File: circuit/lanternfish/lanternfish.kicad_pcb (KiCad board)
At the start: 2 copper layers, 100 x 70 mm, 56 parts, among them J1 Input, J2 Prog, J3 Output, Q1 FQD17P06TM, Q2 PSMN5R6-60YLX, Q3 SI2302DDS-T1-GE3, SW1 SW_Push, SW2 SW_Push, SW3 PEC11R-4215F-S0024, SW6 SW_SPST, U1 MCP7940N-xMS, U2 L7805, U3 ATmega328PB-AU, Y1 ABS25-32.768KHZ-6-1-T

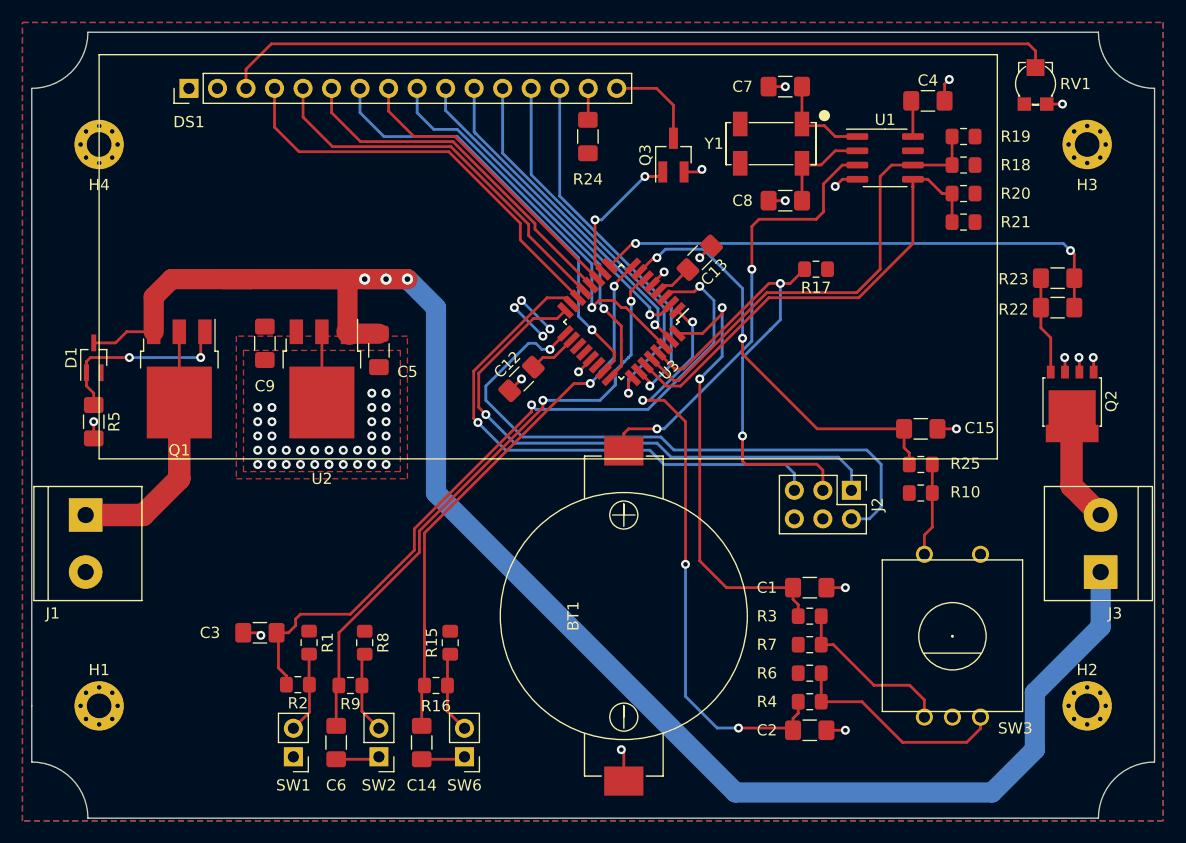
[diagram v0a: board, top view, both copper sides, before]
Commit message: Updated LCD Fixations
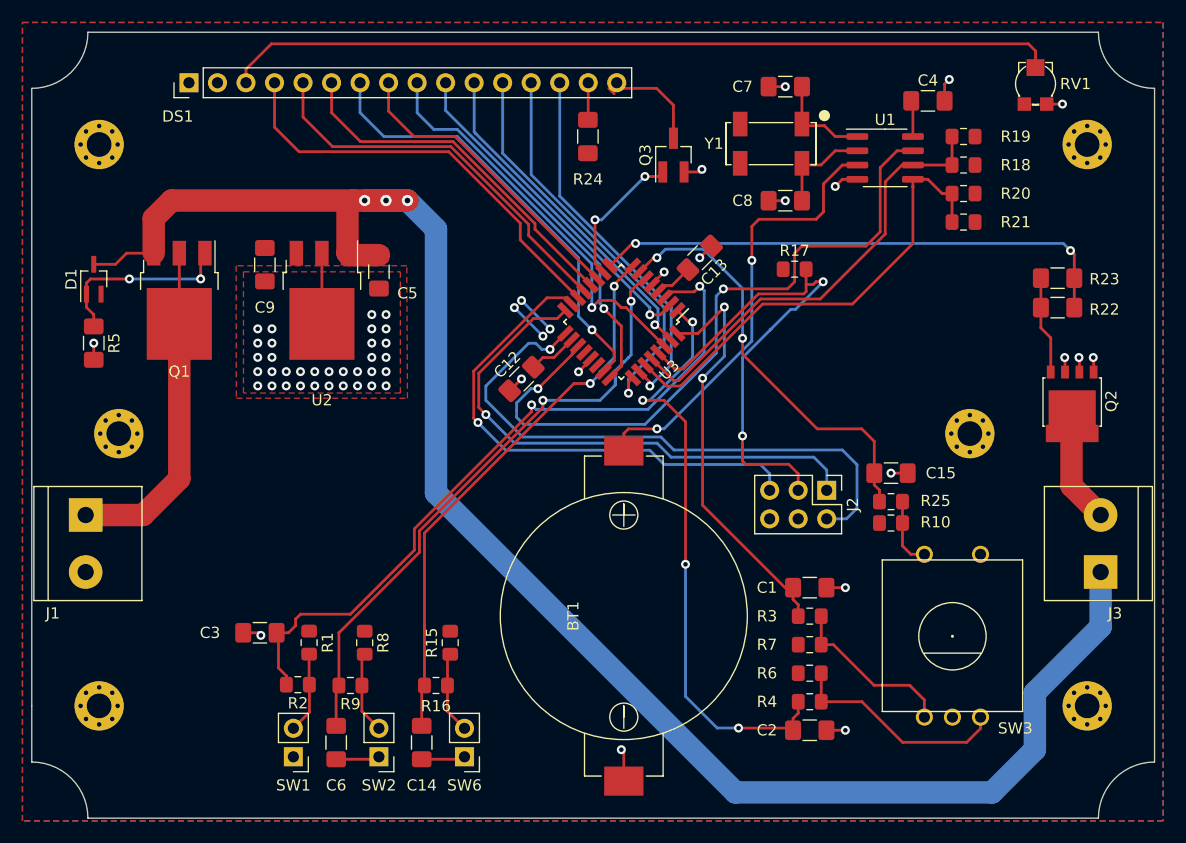
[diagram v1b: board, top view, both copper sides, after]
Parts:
- added REF**: MountingHole_2.2mm_M2_Pad_Via, MountingHole:MountingHole_2.2mm_M2_Pad_Via, F.Cu at (184.6, 95.8)
- added REF**: MountingHole_2.2mm_M2_Pad_Via, MountingHole:MountingHole_2.2mm_M2_Pad_Via, F.Cu at (108.8, 95.8)
- moved C5 7.00 mm to (131.9, 81.3)
- moved C9 7.00 mm to (121.8, 80.7)
- moved D1 7.00 mm to (106.5, 82.0)
- moved Q1 7.00 mm to (114.1, 83.9)
- moved R5 7.00 mm to (106.5, 87.7)
- moved U2 7.00 mm to (126.8, 83.9)
- moved C15 4.76 mm to (177.5, 99.3)
- moved R25 4.24 mm to (177.5, 101.8)
- moved R10 3.77 mm to (177.5, 103.7)
- moved J2 2.20 mm to (171.8, 100.8)
- moved R17 1.91 mm to (168.9, 81.1), turned to 0 degrees
- moved DS1 0.50 mm to (106.5, 62.0)
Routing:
- net /RTC_MSP: track 0.00 -> 62.4 mm, vias 0 -> 2
- net VDD: track 151.3 -> 184.3 mm
- net Net-(J1-Pad1): track 22.8 -> 29.8 mm
- net /RST: track 45.5 -> 49.0 mm
- net /ROT_SW_A: track 40.7 -> 37.5 mm
- net /MOSI: track 48.3 -> 45.8 mm
- net /MISO: track 50.4 -> 48.2 mm
- net /SCL: track 43.4 -> 41.3 mm
- net Net-(R10-Pad2): track 8.29 -> 6.20 mm
- net /SCK: track 55.2 -> 53.2 mm
- net /SW1: track 66.3 -> 65.6 mm
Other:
- net class 25V: trace_width 1.8 -> 2

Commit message: Updated circuit
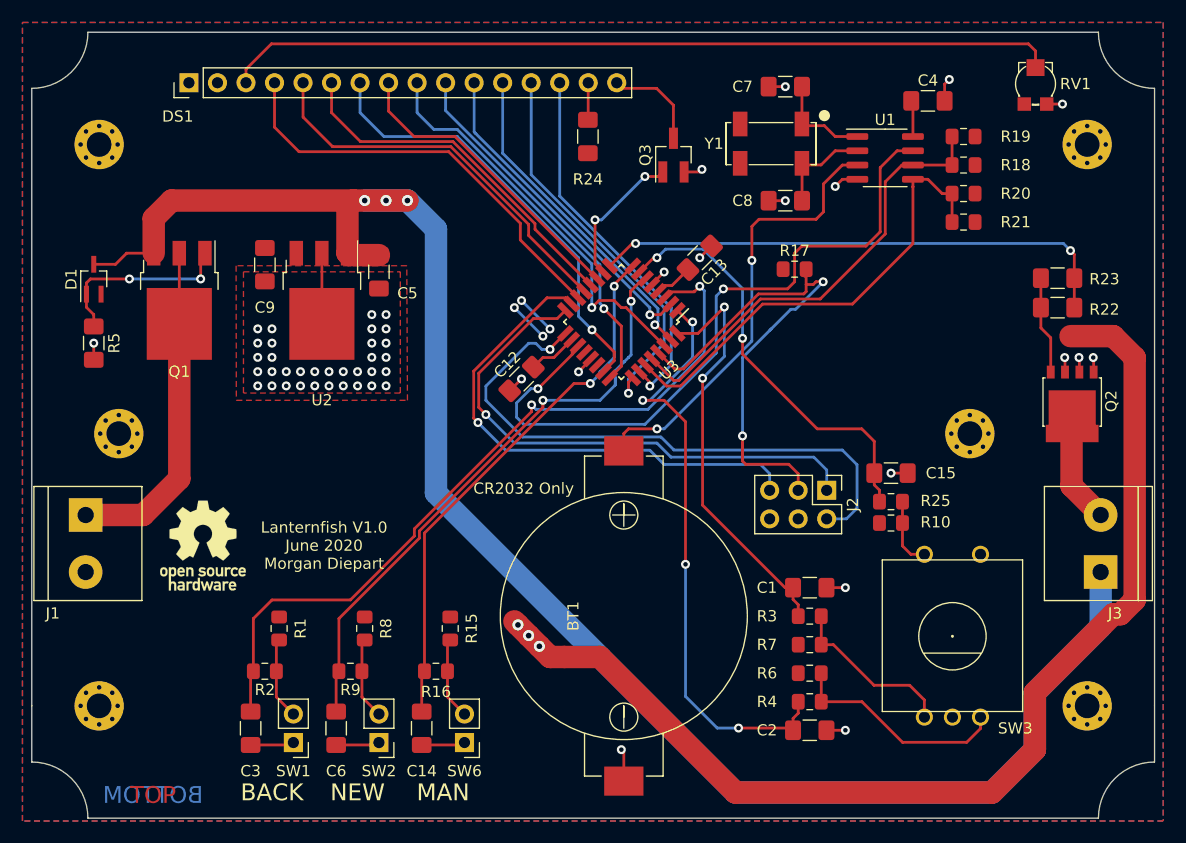
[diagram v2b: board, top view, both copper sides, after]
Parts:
- added REF**: OSHW-Logo_7.5x8mm_SilkScreen, Symbol:OSHW-Logo_7.5x8mm_SilkScreen, F.Cu at (116.2, 105.7)
- moved C3 8.55 mm to (120.5, 122.0), turned to 270 degrees
- moved R2 3.17 mm to (121.8, 116.9)
- moved R1 2.95 mm to (123.0, 113.1)
- moved C14 1.27 mm to (135.7, 122.0)
- moved C6 1.27 mm to (128.1, 122.0)
- moved R15 1.27 mm to (138.3, 113.1)
- moved R16 1.27 mm to (137.0, 116.9)
- moved R8 1.27 mm to (130.7, 113.1)
- moved R9 1.27 mm to (129.4, 116.9)
- moved SW1 1.27 mm to (124.3, 123.3)
- moved SW2 1.27 mm to (131.9, 123.3)
- moved SW6 1.27 mm to (139.5, 123.3)
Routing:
- net GND: track 45.8 -> 147.5 mm, vias 53 -> 55
- net /SW1: track 65.6 -> 69.5 mm
- net /SW_MAN: track 50.5 -> 48.7 mm
- net /SW2: track 55.4 -> 54.2 mm
- net Net-(DS1-Pad16): track 9.30 -> 8.62 mm
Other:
- board text added: "BACK"
- board text added: "BOTTOM"
- board text added: "CR2032 Only"
- board text added: "Lanternfish V1.0 June 2020 Morgan Diepart"
- board text added: "MAN"
- board text added: "NEW"
- board text added: "TOP"

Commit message: Updated circuit
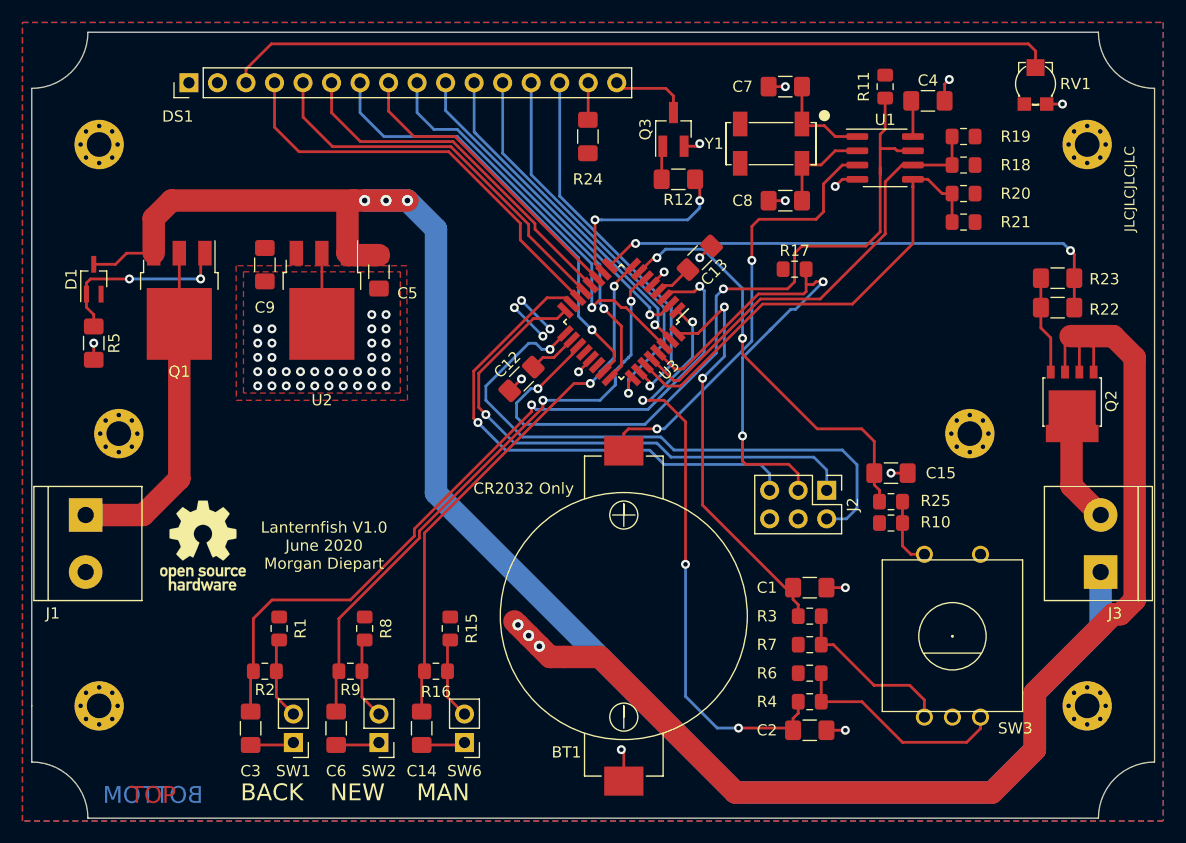
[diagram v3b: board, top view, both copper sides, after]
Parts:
- added R11: 10kR, Resistor_SMD:R_0805_2012Metric_Pad1.15x1.40mm_HandSolder, F.Cu at (177.0, 64.8)
- added R12: 220R, Resistor_SMD:R_1206_3216Metric_Pad1.42x1.75mm_HandSolder, F.Cu at (158.6, 73.1)
- moved Q3 2.29 mm to (158.2, 68.7)
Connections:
- Q3 pad 1: /LCD_BL -> Net-(Q3-Pad1)
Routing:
- net GND: track 147.5 -> 155.5 mm, vias 55 -> 52
- net /RTC_MSP: track 62.4 -> 68.9 mm
- net /LCD_BL: track 13.0 -> 17.7 mm
- net Net-(Q3-Pad1): track 0.00 -> 3.56 mm
- net Net-(DS1-Pad16): track 8.62 -> 6.81 mm
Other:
- board text added: "JLCJLCJLCJLC"
